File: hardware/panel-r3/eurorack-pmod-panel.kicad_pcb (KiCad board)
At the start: 2 copper layers, 15 x 128.5 mm, 11 parts

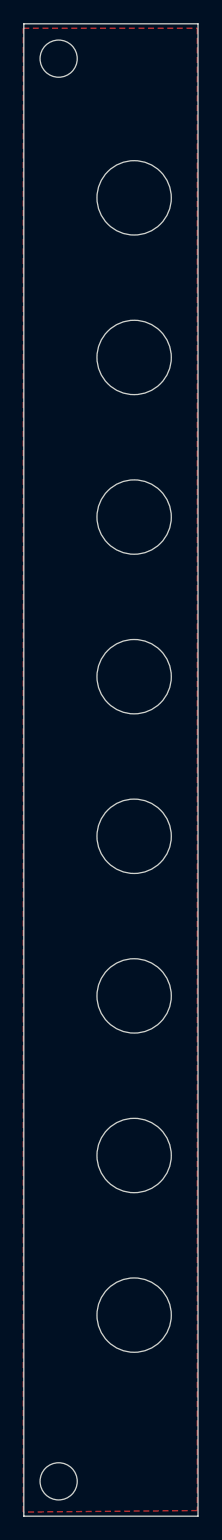
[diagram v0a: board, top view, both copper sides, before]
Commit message: rev3/panel: panel mostly complete
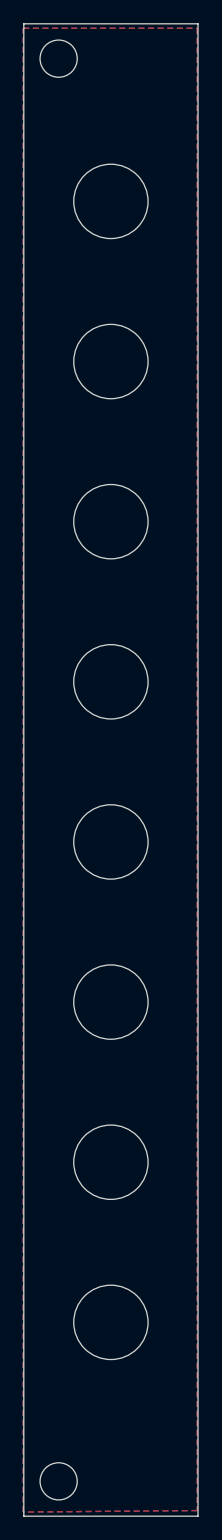
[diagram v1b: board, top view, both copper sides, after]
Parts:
- moved REF** 2.10 mm to (4.50, 111.8)
- moved REF** 2.08 mm to (4.50, 98.0)
- moved REF** 2.07 mm to (4.50, 84.2)
- moved REF** 2.06 mm to (4.50, 70.4)
- moved REF** 2.05 mm to (4.50, 56.7)
- moved REF** 2.04 mm to (4.50, 42.9)
- moved REF** 2.03 mm to (4.50, 29.1)
- moved REF** 2.02 mm to (4.50, 15.3)
- moved REF** 2.00 mm to (-2.00, 9.25)
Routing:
- added copper zone on B.Cu, net (none)
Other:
- board text added: "/////////"
- board text added: "/vk2"
- board text added: "0"
- board text added: "1"
- board text added: "2"
- board text added: "3"
- board text added: "EURO"
- board text added: "INPUTS"
- board text added: "OUTPUTS"
- board text added: "R3"
- board text added: "¬ + ⇒ ⊕ ⊥ ∃ ⊢ ≢ ¬ + ⇒ ⊕ ⊥ ∃ ⊢ ≢"
- board text removed: "BRIDGE"
- board text removed: "VK2 SEB"
- board text removed: "α"
- board text removed: "β"
- board text removed: "γ"
- board text removed: "δ"
